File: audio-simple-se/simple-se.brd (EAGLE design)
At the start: 152.4 x 101.6 mm, 57 parts, among them IC3 10M45, IC4 10M45, J1 6.3VAC, X10 C_FILTER, X11 L_IN, X12 R_IN, X13 6.3VAC, X2 5VAC, X3 CFB_R, X4 CFB_L, X5 L_FILTER, X8 750VAC, X9 CON_B+

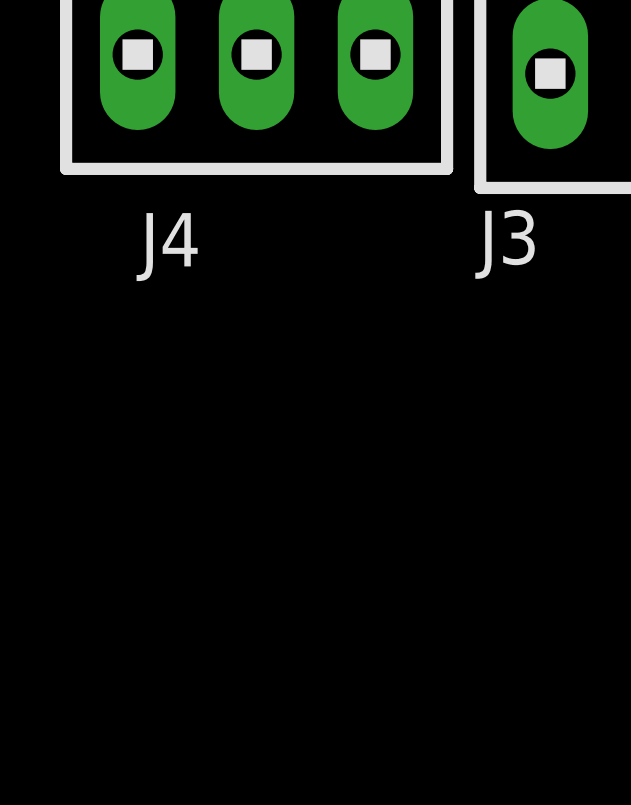
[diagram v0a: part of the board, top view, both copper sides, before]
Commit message: Added M3 PEM nuts to library
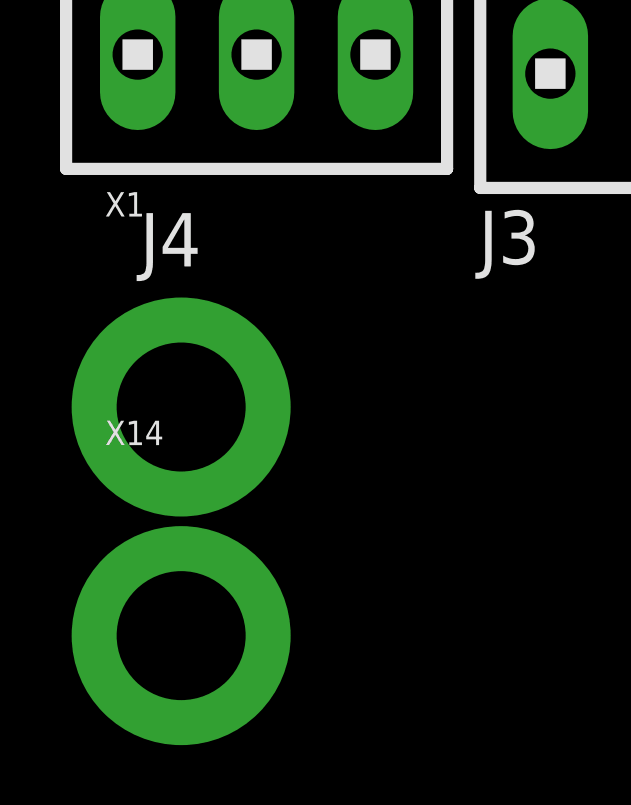
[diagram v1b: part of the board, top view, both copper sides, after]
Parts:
- added X1, X14: PEM-SMTSO-M3, simple-se:SMTSO-M3
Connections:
- net GND: now also X1.P$1, X14.P$1
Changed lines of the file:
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@@
 <?xml version="1.0" encoding="utf-8"?>
 <!DOCTYPE eagle SYSTEM "eagle.dtd">
-<eagle version="6.5.0">
+<eagle version="6.1">
 <drawing>
 <settings>
@@
 </class>
 </classes>
-<designrules name="default">
+<designrules>
 <description language="de">&lt;b&gt;EAGLE Design Rules&lt;/b&gt;
 &lt;p&gt;
@@
 <element name="J3" library="con-amp" package="1X2MTA" value="" x="-35.8775" y="-189.865"/>
 <element name="J4" library="con-amp" package="1X3MTA" value="" x="-47.625" y="-189.23"/>
+<element name="X1" library="simple-se" package="SMTSO-M3" value="PEM-SMTSO-M3" x="-50.165" y="-200.9775"/>
+<element name="X14" library="simple-se" package="SMTSO-M3" value="PEM-SMTSO-M3" x="-50.165" y="-208.5975"/>
 </elements>
 <signals>
@@
 <contactref element="R22" pad="1"/>
 <contactref element="R16" pad="1"/>
+<contactref element="X1" pad="P$1"/>
+<contactref element="X14" pad="P$1"/>
+<wire x1="-50.165" y1="-208.5975" x2="-50.165" y2="-200.9775" width="0" layer="19" extent="1-1"/>
+<wire x1="-4.1275" y1="-183.8325" x2="-50.165" y2="-200.9775" width="0" layer="19" extent="1-1"/>
 <wire x1="-9.2075" y1="-163.5125" x2="-4.1275" y2="-183.8325" width="0" layer="19" extent="1-1"/>
 <wire x1="-9.2075" y1="-151.765" x2="-9.2075" y2="-163.5125" width="0" layer="19" extent="1-1"/>
@@
 <wire x1="0.9525" y1="-46.0375" x2="0.9525" y2="-50.4825" width="0" layer="19" extent="1-1"/>
 <wire x1="4.1275" y1="20.955" x2="0.9525" y2="-46.0375" width="0" layer="19" extent="1-1"/>
+<wire x1="26.035" y1="49.8475" x2="4.1275" y2="20.955" width="0" layer="19" extent="1-1"/>
+<wire x1="22.225" y1="59.055" x2="26.035" y2="49.8475" width="0" layer="19" extent="1-1"/>
+<wire x1="4.1275" y1="84.7725" x2="22.225" y2="59.055" width="0" layer="19" extent="1-1"/>
+<wire x1="4.1275" y1="89.7763" x2="4.1275" y2="84.7725" width="0" layer="19" extent="1-1"/>
+<wire x1="24.765" y1="91.1225" x2="4.1275" y2="89.7763" width="0" layer="19" extent="1-1"/>
+<wire x1="74.295" y1="16.1925" x2="26.035" y2="49.8475" width="0" layer="19" extent="1-1"/>
+<wire x1="75.5904" y1="6.35" x2="74.295" y2="16.1925" width="0" layer="19" extent="1-1"/>
+<wire x1="113.6396" y1="6.35" x2="75.5904" y2="6.35" width="0" layer="19" extent="1-1"/>
+<wire x1="102.5525" y1="46.355" x2="74.295" y2="16.1925" width="0" layer="19" extent="1-1"/>
+<wire x1="104.4829" y1="95.25" x2="102.5525" y2="46.355" width="0" layer="19" extent="1-1"/>
+<wire x1="93.9546" y1="95.25" x2="104.4829" y2="95.25" width="0" layer="19" extent="1-1"/>
 </signal>
 <signal name="N$25">

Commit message: Added SPOX Connectors, Added Heater Linear Supply
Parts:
- removed J3: (no value), con-amp:1X2MTA
- removed J4: (no value), con-amp:1X3MTA
- removed X11: L_IN, con-ptr500:AK500/2
- removed X12: R_IN, con-ptr500:AK500/2
- added C13: 56u, rcl:EB22,5D
- added C14: 15m, rcl:E7,5-18
- added C15, C16: 100n, rcl:C050-055X075
- added C6: 470n, 100V, rcl:C075-063X106
- added IC1: LT4320, simple-se:DIL08
- added IC2: MIC29502WT, Kramnik's Library:TO220-5
- added KK4: SK129-PAD, heatsink:SK129
- added R20: 100R, 1%, rcl:0207/12
- added R24: 412R, 1%, rcl:0207/12
- added S1, S2, S3, S4: (no value), sc_usercreated:DPAK
- added X15: PSU-HV, simple-se:MOLEX-SPOX-5281-3POS
- added X16: OPT-PRI-R, simple-se:MOLEX-SPOX-5281-3POS
- C10: value 0.47uF 100V -> 120u; device rcl:C075-063X106 -> rcl:EB30D
- C8: value 120uF -> 15m; device rcl:EB30D -> rcl:E7,5-18
- C9: value 56uF -> 15m; device rcl:EB22,5D -> rcl:E7,5-18
- J1: value 6.3VAC -> IN-R
- J2: value (none) -> IN-L
- V7: value (none) -> 5AR4
- X10: device con-ptr500:AK500/3 -> simple-se:MOLEX-SPOX-5281-2POS
- X13: value 6.3VAC -> L_FILTER; device con-ptr500:AK500/3 -> simple-se:MOLEX-SPOX-5281-2POS
- X2: value 5VAC -> OPT-PRI-L; device con-ptr500:AK500/2 -> simple-se:MOLEX-SPOX-5281-3POS
- X3: value CFB_R -> PSU-STANDBY; device con-ptr500:AK500/2 -> simple-se:MOLEX-SPOX-5281-2POS
- X4: value CFB_L -> TRIODE-UL-SW-R; device con-ptr500:AK500/2 -> simple-se:MOLEX-SPOX-5281-3POS
- X5: value L_FILTER -> TRIODE-UL-SW-L; device con-ptr500:AK500/2 -> simple-se:MOLEX-SPOX-5281-3POS
- X6: value (none) -> CFB-L; device con-ptr500:AK500/3 -> simple-se:MOLEX-SPOX-5281-2POS
- X7: value (none) -> CFB-R; device con-ptr500:AK500/3 -> simple-se:MOLEX-SPOX-5281-2POS
- X8: value 750VAC -> PSU-5VAC; device con-ptr500:AK500/3 -> simple-se:MOLEX-SPOX-5281-2POS
- X9: value CON_B+ -> PSU-6V3AC; device con-ptr500:AK500/2 -> simple-se:MOLEX-SPOX-5281-3POS
- moved X4 529.9 mm to (-161.9, -361.3), flipped to the top
- moved X7 517.8 mm to (-187.3, -361.3), flipped to the top, turned to 0 degrees
- moved C8 516.9 mm to (-184.2, -386.7), flipped to the top, turned to 0 degrees
- moved X6 498.7 mm to (-175.9, -361.3), flipped to the top, turned to 0 degrees
- moved C9 496.6 mm to (-184.2, -405.1), flipped to the top, turned to 0 degrees
- moved X3 435.9 mm to (-104.1, -294.3), flipped to the top
- moved C10 399.8 mm to (-99.1, -318.1), flipped to the top, turned to 0 degrees
- moved X9 394.1 mm to (-68.3, -279.7), flipped to the top
- moved X10 374.5 mm to (-81.9, -279.7), flipped to the top, turned to 0 degrees
- moved X13 359.8 mm to (-93.0, -279.7), flipped to the top, turned to 0 degrees
- moved X5 357.9 mm to (-90.5, -294.3), flipped to the top, turned to 0 degrees
- moved X2 294.1 mm to (-57.1, -250.5), flipped to the top, turned to 0 degrees
- moved X14 281.5 mm to (112.4, 21.3)
- moved X1 256.0 mm to (76.8, 21.3)
- moved X8 236.1 mm to (-59.7, -206.4), flipped to the top, turned to 0 degrees
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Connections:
- removed net N$23 (its old number): R23.1, X7.2
- removed net N$38: V1.9, V5.7, V6.7, X13.1
- new net N$29: R23.1, X4.P$2
- new net N$42: IC1.3, S4.1
- new net N$43: IC1.2, S2.1
- new net N$44: IC1.1, S2.3, S3.4, X9.P$1
- new net N$45: IC1.4, S3.1
- new net N$46: C14.-, C15.2, C16.2, C8.-, C9.-, IC1.5, IC2.3, R20.1, S3.3, S4.3, V1.9, V5.7, V6.7
- new net N$47: C14.+, C16.1, C6.1, IC2.4, R16.2, R21.1, R24.1, V1.4, V1.5, V5.2, V6.2
- new net N$49: IC2.5, R20.2, R24.2
- new net NC_6V3AC_CT: X9.P$2
- new net OPT-MINUS-L: V5.3, X2.P$2, X5.P$1
- new net OPT-UL-TAP-L: X2.P$3, X5.P$3
- net B+: now also C10.+, X10.P$1, X13.P$2, X16.P$1, X2.P$1; no longer C8.+, X10.3, X5.1, X9.1, X9.2
- net GND: now also C10.-, C13.-, C6.2, J1.2, J2.2, X10.P$2, X3.P$2, X6.P$2, X7.P$2; no longer C10.2, C8.-, C9.-, X10.1, X10.2, X11.2, X12.1, X3.1, X4.2, X8.2
- net LOUT_PLATE: now also X16.P$2, X4.P$1; no longer X7.3
- net LOUT_SCREEN: now also X16.P$3, X4.P$3; no longer X7.1
- net N$10: now also J2.1; no longer X12.2
- net N$19: now also X6.P$1; no longer X3.2
- net N$21: now also X5.P$2; no longer X6.2
- net N$22: now also X15.P$2, X3.P$1; no longer V5.3, X6.1
- net N$25: now also C13.+, X13.P$1, X8.P$2; no longer C9.+, X2.1, X5.2
- net N$26: now also X15.P$1; no longer X8.1
- net N$27: now also IC1.7, S1.1; no longer V1.4, V1.5, V5.2, V6.2, X13.3
- net N$33: now also X15.P$3; no longer X8.3
- net N$34: now also IC1.8, S1.3, S4.4, X9.P$3; no longer X6.3
- net N$35: now also X8.P$1; no longer X2.2
- net N$40: now also X7.P$1; no longer X4.1
- net N$41: now also C15.1, C8.+, C9.+, IC1.6, IC2.1, IC2.2, S1.4, S2.4; no longer C10.1, R16.2, R21.1, X13.2
- net N$9: now also J1.1; no longer X11.1
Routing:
- net N$38: track 217.3 -> 0.00 mm, vias 3 -> 0
- net N$27: track 176.7 -> 0.00 mm
- net B+: track 160.6 -> 0.00 mm
- net N$25: track 42.3 -> 0.00 mm
- net N$22: track 42.2 -> 0.00 mm
- net N$2: track 41.3 -> 0.00 mm
- net N$35: track 39.4 -> 0.00 mm
- net N$32: track 36.5 -> 0.00 mm
- net N$30: track 31.1 -> 0.00 mm
- net N$21: track 27.2 -> 0.00 mm
- net N$33: track 19.9 -> 0.00 mm
- net N$16: track 18.0 -> 0.00 mm
- net N$39: track 12.7 -> 0.00 mm
- net N$19: track 12.4 -> 0.00 mm
- net N$40: track 12.4 -> 0.00 mm
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- removed copper zone on layer 1, net B+
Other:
- board text removed: "B+"
- board text removed: "CFB"
- board text removed: "GND"

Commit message: Added Quench Circuit Directory
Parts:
- added B1: RECTIFIER-GBU4, rectifier:GBU4
- added C17: 100n, rcl:C102-043X133
- added C18: 1500u, 63V, rcl:E5-13
- added C19, C20: 100n, 630V, rcl:C150-072X183
- added C21: 100n, rcl:C150-072X183
- added C22: 10u, 630V, rcl:C150-072X183
- added D10: 1N5342, diode:DO35Z10
- added D8, D9: 1N4007, diode:DO41-10
- added IC5, IC6: 10M45, simple-se:TO220V
- added IC9: LM317, v-reg:317TS
- added J4: STAGE1-SEL-L, con-amp:1X3MTA
- added J5: STAGE1-SEL-R, con-amp:1X3MTA
- added KK3: SK129-PAD, heatsink:SK129
- added R25: 10R, 3W, rcl:0617/17
- added R26: 191R, rcl:0309/12
- added R27: R_FILTER, rcl:0922/22
- added R28: 1R, rcl:0309/12
- added R29, R31: 1k, rcl:0309/12
- added R30: 1k, pot:S64W
- added R32: 68.1k, rcl:0309/12
- added R34, R35: 10R, rcl:0309/12
- added R36: 6k2, rcl:0309/12
- added T3: BUL416T, transistor:TO220V
- added X11: PEM-SMTSO-M3, simple-se:SMTSO-M3
- added X12: OPT-SEC-L, simple-se:MOLEX-SPOX-5281-2POS
- added X17: SPKR-L, simple-se:MOLEX-SPOX-5281-2POS
- added X18: SPKR-R, simple-se:MOLEX-SPOX-5281-2POS
- added X19: CFB-SW-R, simple-se:MOLEX-SPOX-5281-3POS
- C1: value 1500u 63V -> 1500u, 6.3V
- C11, C7: value 0.1uF 400V -> 100n, 630V; device rcl:C102-064X133 -> rcl:C150-072X183
- C14: value 15m -> 15m, 10V
- C2: value 1500u 6.3V -> 1500u, 6.3V
- C3: value 1500u 63V -> 1500u, 63V
- C4: value 1500u 63V -> 100n, 630V; device rcl:E5-13 -> rcl:C150-072X183
- C8, C9: value 15m -> 15m, 16V
- R1, R10, R11, R12, R13, R15, R2, R20, R24, R3, R4, R5, R6, R7, R8, R9: device rcl:0207/12 -> rcl:0309/12
- X15: value PSU-HV -> PSU-HV-IN
- X3: value PSU-STANDBY -> PSU-STANDBY-SW
- X6: value CFB-L -> CFB-SW-L; device simple-se:MOLEX-SPOX-5281-2POS -> simple-se:MOLEX-SPOX-5281-3POS
- X7: value CFB-R -> OPT-SEC-R
- X8: value PSU-5VAC -> PSU-5VAC-IN
- X9: value PSU-6V3AC -> PSU-6V3AC-IN
- moved KK4 664.1 mm to (31.1, 148.6)
- moved IC2 560.1 mm to (31.1, 148.6), turned to 180 degrees
- moved C14 493.4 mm to (-101.6, 62.9)
- moved C15 493.4 mm to (-104.8, 48.3)
- moved C16 493.4 mm to (-106.0, 40.0)
- moved C8 493.4 mm to (-101.6, 99.7)
- moved C9 493.4 mm to (-101.6, 81.3)
- moved R20 493.4 mm to (-102.9, 33.7)
- moved R24 493.4 mm to (-102.9, 29.2)
- moved X4 493.4 mm to (-79.4, 125.1)
- moved C10 468.1 mm to (-43.8, 146.7)
- moved C13 461.8 mm to (-43.8, 117.5)
- moved C4 443.6 mm to (-181.6, -249.6), flipped to the top
- moved X9 358.5 mm to (6.99, 70.8), flipped to the bottom, turned to 270 degrees
- moved X16 346.4 mm to (-147.6, 72.1)
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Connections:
- net LOUT_PLATE renamed OPT-MINUS-R
- net LOUT_SCREEN renamed OPT-UL-TAP-R
- net N$12 renamed SCREEN-GRID-L
- net N$21 renamed SCREEN-GRID-CONN-L
- net N$23 renamed SCREEN-GRID-R
- net N$29 renamed SCREEN-GRID-CONN-R
- new net HV_LFILT: C10.+, D9.C, R27.1, R35.2, R36.2, X10.P$1, X13.P$2
- new net HV_RECT: C13.+, R27.2, V7.2, X13.P$1, X8.P$2
- new net N$12: B1.+, B1.-
- new net N$21: B1.AC1, C17.1, R25.2, X11.P$1
- new net N$23: X12.P$1, X17.P$1, X6.P$1
- new net N$24: R35.1, T3.2
- new net N$28: C21.1, R34.2, T3.3
- new net N$29: C20.1, C21.2, IC9.3, R34.1
- new net N$36: X19.P$2
- new net N$37: X18.P$1, X19.P$1, X7.P$1
- new net N$38: C22.1, R28.1
- new net N$48: D10.C, R36.1, T3.1
- new net N$50: IC5.1, R29.2
- new net N$51: IC5.2, R14.2
- new net N$52: C12.2, J4.2
- new net N$53: IC4.2, IC6.3
- new net N$54: IC6.1, R31.2
- new net N$55: C5.1, J5.2
- net B+: now also C19.1, D10.A, D8.C, D9.A, IC9.2, R26.2, R30.E; no longer C10.+, X10.P$1, X13.P$2
- net GND: now also B1.AC2, C17.2, C19.2, C20.2, C22.2, C4.2, R25.1, R32.1, X12.P$2, X17.P$2, X18.P$2, X19.P$3, X6.P$3; no longer X6.P$2
- net N$14: now also C12.1; no longer C12.2
- net N$15: now also C1.+; no longer C2.+
- net N$16: now also C2.+; no longer C1.+
- net N$17: now also IC6.2; no longer IC4.2
- net N$18: now also IC5.3; no longer R14.2
- net N$19: now also C18.-, X6.P$2; no longer C3.-, X6.P$1
- net N$2: now also J4.3; no longer C12.1
- net N$25: now also C4.1, D8.A, IC9.1, R26.1, R28.2, R30.A, R30.S, R32.2; no longer C13.+, V7.2, X13.P$1, X8.P$2
- net N$30: now also C11.2, C18.+; no longer C3.+, C7.2
- net N$31: now also C7.1; no longer C11.1
- net N$32: now also C3.+, C7.2; no longer C11.2, C4.+
- net N$39: now also C11.1; no longer C7.1
- net N$4: now also J5.3; no longer C5.1
- net N$40: now also C3.-; no longer C4.-, X7.P$1
- net N$5: now also J5.1, R31.1
- net N$7: now also J4.1, R29.1
